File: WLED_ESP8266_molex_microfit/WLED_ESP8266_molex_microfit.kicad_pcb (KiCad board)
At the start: 2 copper layers, 50 x 65 mm, 62 parts, among them J1 Molex Micro-fit 2x1, J2 Molex Micro-fit 3x1, J3 Molex Micro-fit 2x1, J4 Molex Micro-fit 2x1, J6 Molex Micro-fit 2x1, J7 Molex Micro-fit 3x1, J8 Molex Micro-fit 3x1, Q1 AO3401A, Q2 AO3401A, U1 ESP-12F, U2 TPS54331DDAR, U3 TXS0102DCT, U4 TXS0102DCT, U6 ME6211A33M3G-N

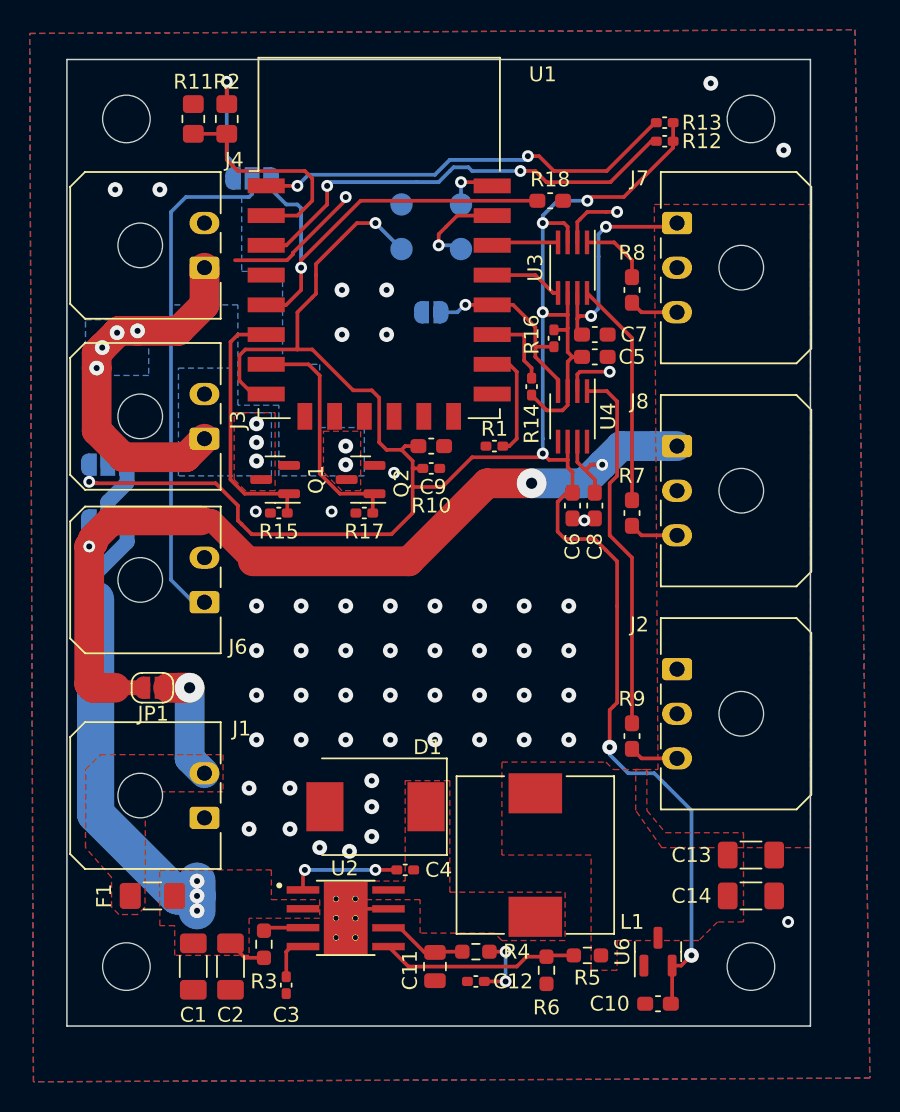
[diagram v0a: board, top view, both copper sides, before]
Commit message: USB added
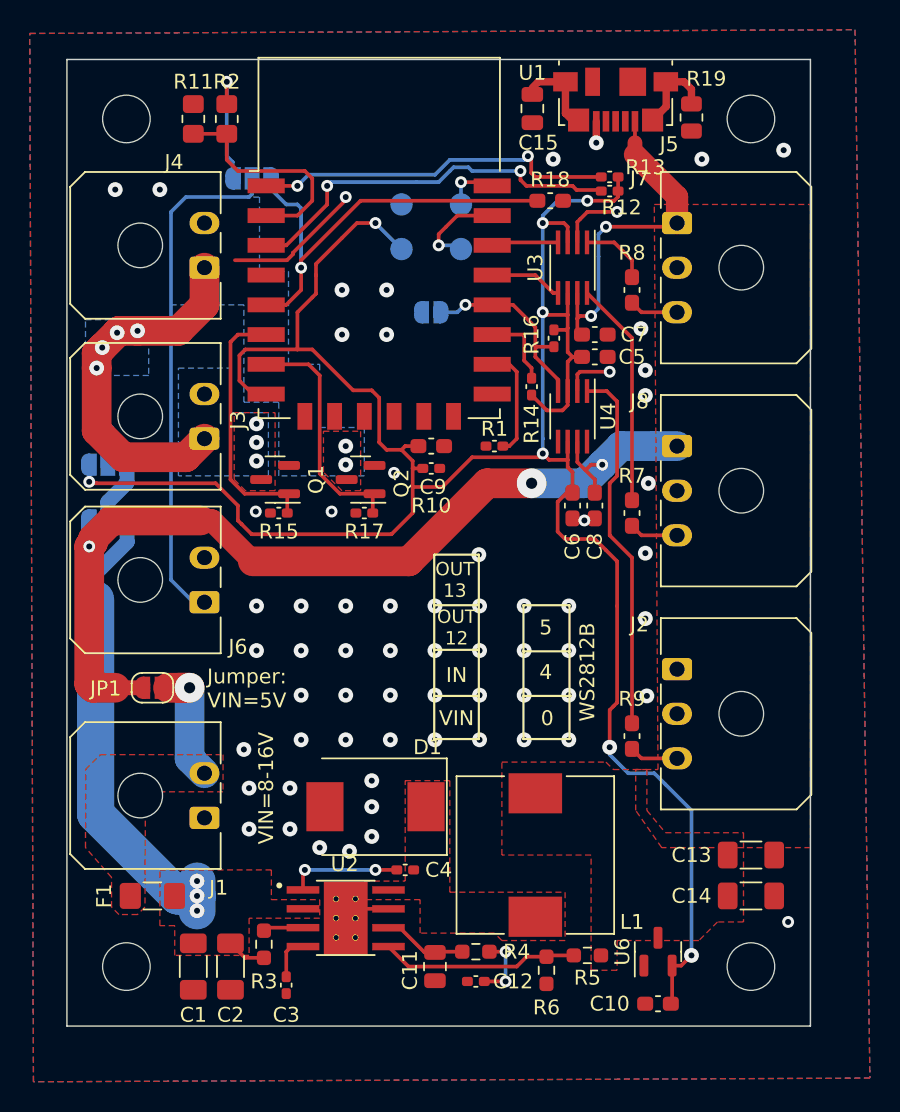
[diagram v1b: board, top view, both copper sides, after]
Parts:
- added C15: 0.01uF, Capacitor_SMD:C_0805_2012Metric, F.Cu at (149.2, 68.9)
- added J5: USB_B_Micro, Connector_USB:USB_Micro-B_Molex_47346-0001, F.Cu at (154.8, 68.3)
- added R19: 1M, Resistor_SMD:R_0805_2012Metric, F.Cu at (159.9, 69.5)
- moved R13 5.20 mm to (154.4, 73.5)
- moved R12 4.99 mm to (154.4, 74.4)
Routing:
- net GND1: track 0.00 -> 11.9 mm
- net +5V: track 79.9 -> 87.9 mm
- net +3V3: track 168.1 -> 162.7 mm
- net RST: track 28.8 -> 24.5 mm
- net EN: track 30.7 -> 26.5 mm
- net GND: track 20.3 -> 21.7 mm, vias 57 -> 66
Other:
- board text added: "+5V"
- board text added: "0"
- board text added: "3V3"
- board text added: "4"
- board text added: "5"
- board text added: "Analog_IN"
- board text added: "Digital_IN"
- board text added: "GND 3V3"
- board text added: "GPIO_0 - GND"
- board text added: "IN"
- board text added: "Jumper: VIN=5V"
- board text added: "OUT 12"
- board text added: "OUT 13"
- board text added: "TX RX"
- board text added: "VIN"
- board text added: "VIN=8-16V"
- board text added: "WS2812B"

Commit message: Issue 28.01.Yannik_part1
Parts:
- R1, R10, R12, R13, R14, R15, R16, R17: footprint Capacitor_SMD:C_0402_1005Metric_Pad0.74x0.62mm_HandSolder -> Resistor_SMD:R_0402_1005Metric_Pad0.72x0.64mm_HandSolder
- R18, R7, R8, R9: footprint Capacitor_SMD:C_0603_1608Metric_Pad1.08x0.95mm_HandSolder -> Resistor_SMD:R_0603_1608Metric_Pad0.98x0.95mm_HandSolder
- moved R10 0.10 mm to (142.3, 93.1)
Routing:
- net +3V3: track 162.7 -> 168.4 mm

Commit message: feedback implemented
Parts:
- removed TP1: +3.3V, TestPoint:TestPoint_Pad_D1.5mm
- removed TP2: TX, TestPoint:TestPoint_Pad_D1.5mm
- removed TP3: RX, TestPoint:TestPoint_Pad_D1.5mm
- removed TP4: GND, TestPoint:TestPoint_Pad_D1.5mm
- added J9: Conn_01x04_Male, Connector_PinHeader_2.54mm:PinHeader_1x04_P2.54mm_Vertical, F.Cu at (153.7, 107.6)
- moved C10 30.4 mm to (149.2, 99.9)
- moved U6 29.7 mm to (149.2, 97.1)
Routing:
- net +3V3: track 168.4 -> 132.7 mm, vias 8 -> 5
- net TX: track 3.70 -> 38.4 mm
- net RX: track 6.47 -> 40.2 mm
- net +5V: track 87.9 -> 90.0 mm
- net GND: vias 66 -> 74
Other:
- board text added: "GND RX TX 3V3"

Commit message: V2 in production
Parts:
- L1: footprint Inductor_SMD:L_10.4x10.4_H4.8 -> Inductor_SMD:L_7.3x7.3_H3.5
